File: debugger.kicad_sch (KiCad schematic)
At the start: 16 parts, among them J10 TC_SWD, J6 MCU_SWD, U6 ATSAMD11

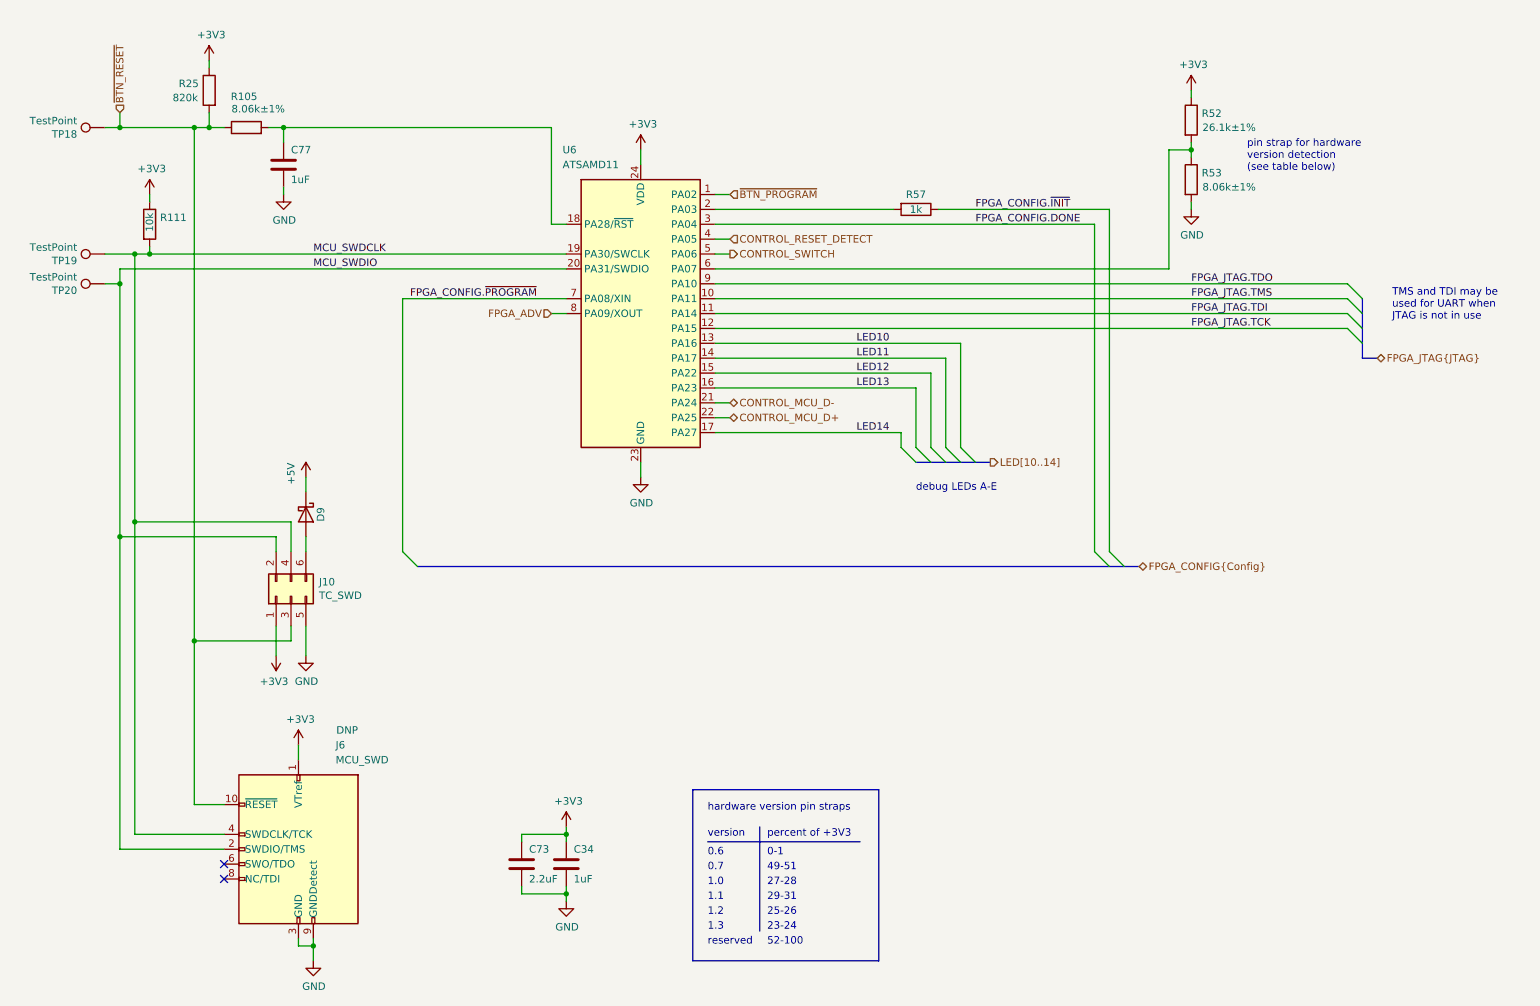
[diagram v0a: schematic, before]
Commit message: add first round of hits on lcsc
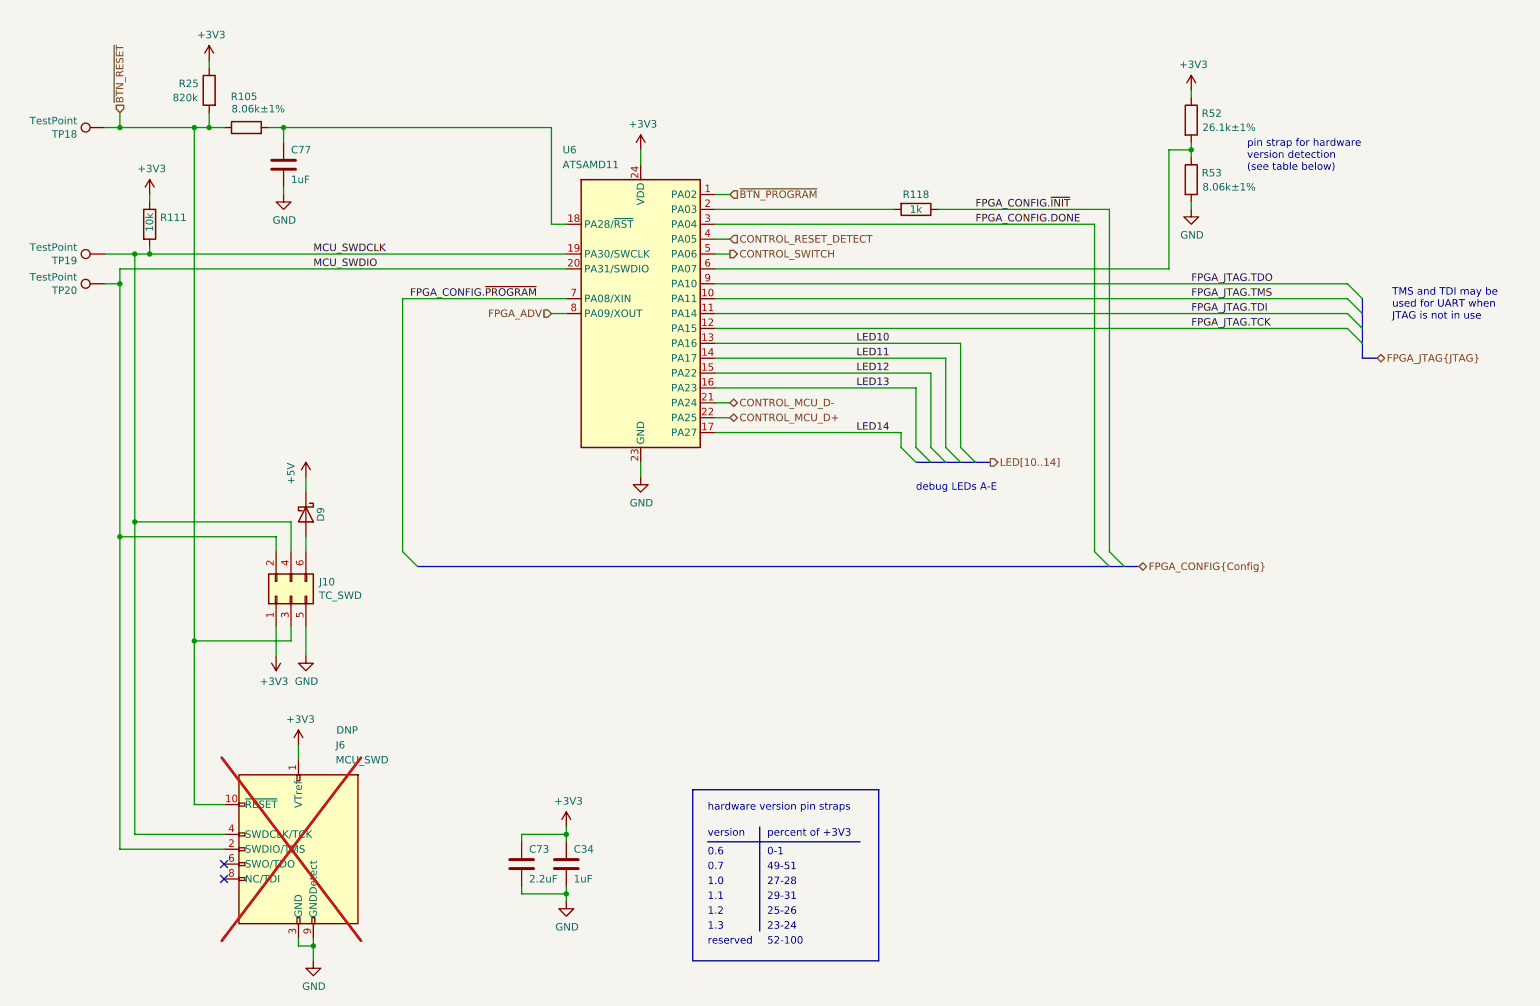
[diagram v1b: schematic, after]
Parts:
- C34, C77: LCSC# (none) -> C318573
- C73: LCSC# (none) -> C1607
- D9: LCSC# (none) -> C22365186
- J6: now not fitted
- R105, R53: LCSC# (none) -> C2076955
- R111: LCSC# (none) -> C60489
- R118: renamed from R57; LCSC# (none) -> C105637
- R25: LCSC# (none) -> C137838
- R52: LCSC# (none) -> C155697
